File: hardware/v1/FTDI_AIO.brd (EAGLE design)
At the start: 49.5 x 49.5 mm, 45 parts, among them IC1 MCP1702-3.3, IC2 FT232RL, X1 ISP, X2 USB-A-H, X3 UART

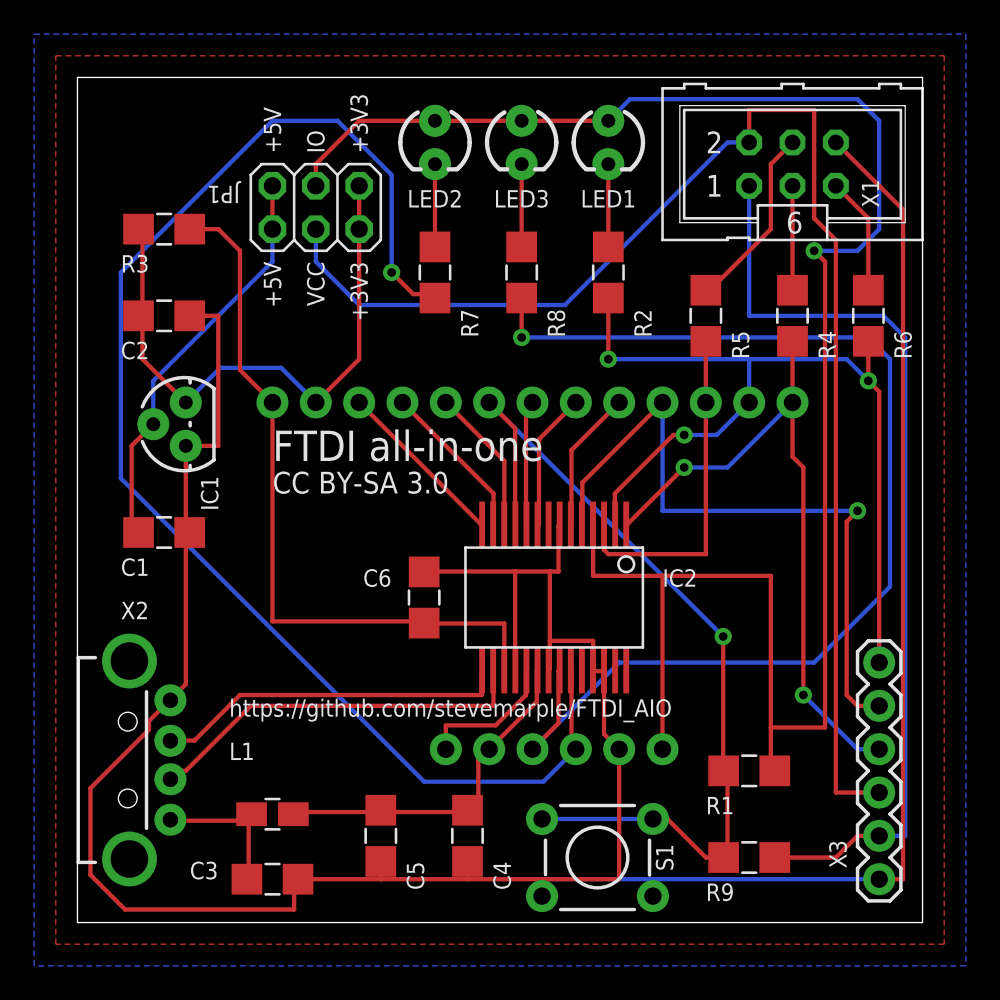
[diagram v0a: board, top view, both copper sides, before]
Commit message: Moved jumper block. Updated FT232RL package.
Jumper block moved to make room for larger text describing jumper options.
Updated FT232RL so that silkscreen does not printer over pads.
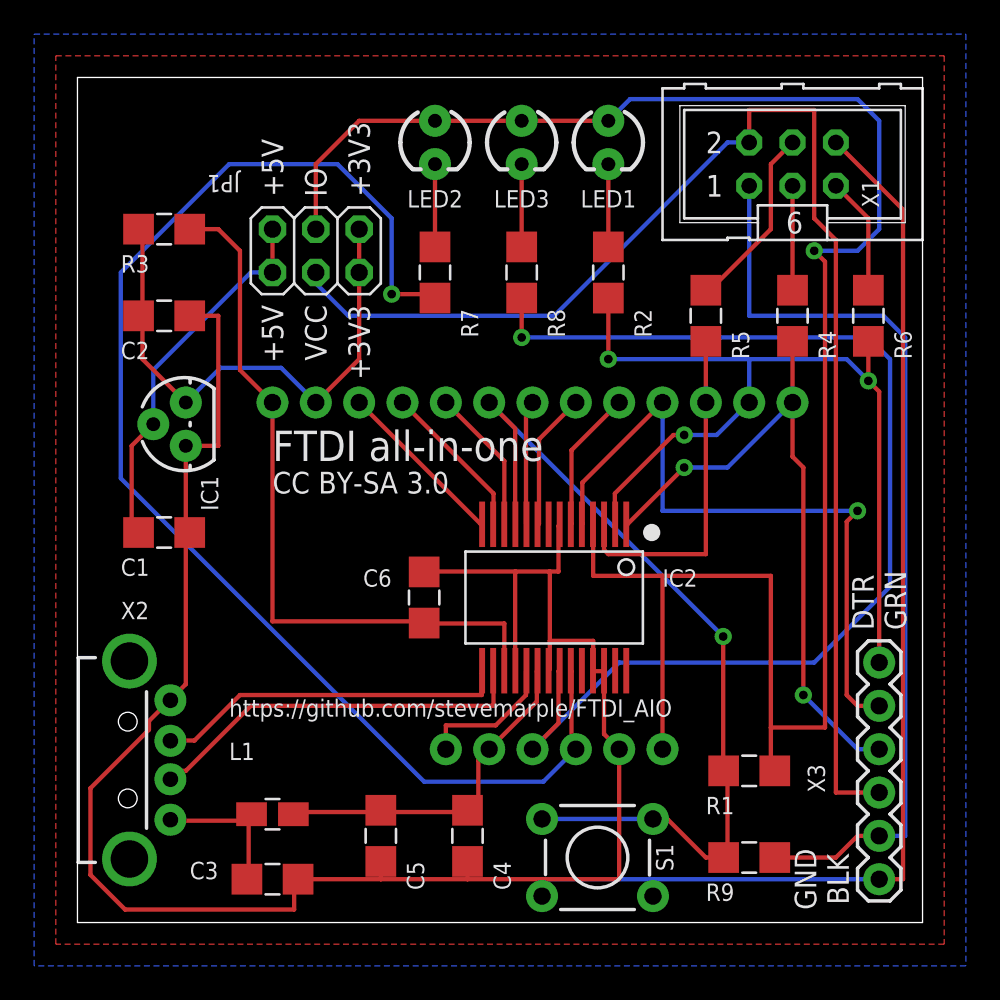
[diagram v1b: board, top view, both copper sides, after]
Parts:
- moved JP1 2.54 mm to (14.0, 39.4)
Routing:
- net N$11: track 81.5 -> 78.6 mm
- net +3V3: track 35.0 -> 32.4 mm
- net VCC: track 113.7 -> 116.3 mm
- net +5V: track 24.2 -> 22.5 mm
- net EXT_VCC: track 81.1 -> 79.8 mm
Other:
- board text added: "DTR GRN"
- board text added: "GND BLK"
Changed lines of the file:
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@@
 <wire x1="49.53" y1="49.53" x2="0" y2="49.53" width="0" layer="20"/>
 <wire x1="0" y1="49.53" x2="0" y2="0" width="0" layer="20"/>
-<text x="13.97" y="38.735" size="1.016" layer="121" ratio="10" rot="R90" align="center-right">VCC</text>
-<text x="13.97" y="45.085" size="1.016" layer="121" ratio="10" rot="R90" align="center-left">IO</text>
-<text x="11.43" y="45.085" size="1.016" layer="121" ratio="10" rot="R90" align="center-left">+5V</text>
-<text x="16.51" y="45.085" size="1.016" layer="121" ratio="10" rot="R90" align="center-left">+3V3</text>
-<text x="11.43" y="38.735" size="1.016" layer="121" ratio="10" rot="R90" align="center-right">+5V</text>
-<text x="16.51" y="38.735" size="1.016" layer="121" ratio="10" rot="R90" align="center-right">+3V3</text>
+<text x="13.97" y="36.195" size="1.27" layer="121" ratio="10" rot="R90" align="center-right">VCC</text>
+<text x="13.97" y="42.545" size="1.27" layer="121" ratio="10" rot="R90" align="center-left">IO</text>
+<text x="11.43" y="42.545" size="1.27" layer="121" ratio="10" rot="R90" align="center-left">+5V</text>
+<text x="16.51" y="42.545" size="1.27" layer="121" ratio="10" rot="R90" align="center-left">+3V3</text>
+<text x="11.43" y="36.195" size="1.27" layer="121" ratio="10" rot="R90" align="center-right">+5V</text>
+<text x="16.51" y="36.195" size="1.27" layer="121" ratio="10" rot="R90" align="center-right">+3V3</text>
 <text x="11.43" y="27.051" size="1.778" layer="121" ratio="14">FTDI all-in-one</text>
 <text x="41.91" y="14.605" size="1.016" layer="122" ratio="10" rot="MR0">https://github.com/stevemarple/FTDI_AIO</text>
@@
 Attribution-ShareAlike 3.0</text>
 <text x="8.89" y="12.065" size="1.016" layer="121" ratio="10">https://github.com/stevemarple/FTDI_AIO</text>
+<circle x="33.655" y="22.86" radius="0.508" width="0" layer="121"/>
+<text x="46.99" y="17.145" size="1.27" layer="121" ratio="10" rot="R90" align="center-left">DTR
+GRN</text>
+<text x="45.212" y="2.54" size="1.27" layer="121" ratio="10" rot="R90" align="bottom-center">GND
+BLK</text>
 </plain>
 <attributes>
@@
 </element>
 <element name="X3" library="SparkFun" package="1X06" value="UART" x="46.99" y="15.24" smashed="yes" rot="R270">
-<attribute name="NAME" x="45.085" y="3.175" size="1.016" layer="25" ratio="10" rot="R90"/>
-<attribute name="VALUE" x="45.085" y="6.35" size="1.016" layer="27" ratio="10" rot="R90"/>
+<attribute name="NAME" x="43.815" y="7.62" size="1.016" layer="25" ratio="10" rot="R90"/>
+<attribute name="VALUE" x="45.085" y="7.62" size="1.016" layer="27" ratio="10" rot="R90"/>
 </element>
 <element name="R7" library="SteveMarple" package="1206-HAND" value="560R" x="20.955" y="38.1" smashed="yes" rot="R90">
@@
 <attribute name="VALUE" x="40.005" y="1.27" size="1.016" layer="27" ratio="10"/>
 </element>
-<element name="JP1" library="pinhead" package="2X03" value="POWER" x="13.97" y="41.91" smashed="yes">
-<attribute name="NAME" x="9.525" y="43.18" size="1.016" layer="25" ratio="10" rot="SR180"/>
-<attribute name="VALUE" x="9.525" y="44.45" size="1.016" layer="27" ratio="10" rot="SR180"/>
+<element name="JP1" library="pinhead" package="2X03" value="POWER" x="13.97" y="39.37" smashed="yes">
+<attribute name="NAME" x="9.525" y="43.815" size="1.016" layer="25" ratio="10" rot="SR180"/>
+<attribute name="VALUE" x="9.525" y="45.085" size="1.016" layer="27" ratio="10" rot="SR180"/>
 </element>
 <element name="X1" library="SteveMarple" package="CONN-HARTING-ML6" value="ISP" x="41.91" y="44.45" smashed="yes">
@@
 <wire x1="30.226" y1="23.241" x2="30.215" y2="23.341" width="0.254" layer="1"/>
 <wire x1="16.51" y1="46.99" x2="13.97" y2="44.45" width="0.254" layer="1"/>
-<wire x1="13.97" y1="44.45" x2="13.97" y2="43.18" width="0.254" layer="1"/>
+<wire x1="13.97" y1="44.45" x2="13.97" y2="40.64" width="0.254" layer="1"/>
 <wire x1="20.955" y1="46.99" x2="16.51" y2="46.99" width="0.254" layer="1"/>
 <wire x1="20.955" y1="46.99" x2="26.035" y2="46.99" width="0.254" layer="1"/>
@@
 <contactref element="IC2" pad="23"/>
 <contactref element="U$14" pad="1"/>
-<wire x1="19.685" y1="36.83" x2="20.955" y2="36.83" width="0.254" layer="1"/>
 <wire x1="20.955" y1="36.83" x2="20.955" y2="36.601" width="0.254" layer="1"/>
-<wire x1="18.415" y1="38.1" x2="19.685" y2="36.83" width="0.254" layer="1"/>
-<wire x1="18.415" y1="43.815" x2="18.415" y2="38.1" width="0.254" layer="16"/>
-<wire x1="11.43" y1="46.99" x2="15.24" y2="46.99" width="0.254" layer="16"/>
-<wire x1="15.24" y1="46.99" x2="18.415" y2="43.815" width="0.254" layer="16"/>
-<wire x1="2.54" y1="38.1" x2="11.43" y2="46.99" width="0.254" layer="16"/>
+<wire x1="18.415" y1="36.83" x2="20.955" y2="36.83" width="0.254" layer="1"/>
+<wire x1="18.415" y1="41.275" x2="18.415" y2="36.83" width="0.254" layer="16"/>
+<wire x1="8.89" y1="44.45" x2="15.24" y2="44.45" width="0.254" layer="16"/>
+<wire x1="15.24" y1="44.45" x2="18.415" y2="41.275" width="0.254" layer="16"/>
+<wire x1="2.54" y1="38.1" x2="8.89" y2="44.45" width="0.254" layer="16"/>
 <wire x1="2.54" y1="26.035" x2="2.54" y2="38.1" width="0.254" layer="16"/>
 <wire x1="20.32" y1="8.255" x2="2.54" y2="26.035" width="0.254" layer="16"/>
@@
 <wire x1="29.21" y1="10.16" x2="28.956" y2="10.414" width="0.254" layer="1"/>
 <wire x1="28.956" y1="14.732" x2="28.915" y2="14.759" width="0.254" layer="1"/>
-<via x="18.415" y="38.1" extent="1-16" drill="0.508"/>
+<via x="18.415" y="36.83" extent="1-16" drill="0.508"/>
 </signal>
 <signal name="N$12">
@@
 <contactref element="IC1" pad="2"/>
 <contactref element="C1" pad="1"/>
-<wire x1="11.43" y1="43.18" x2="11.43" y2="40.64" width="0.254" layer="1"/>
+<wire x1="11.43" y1="40.64" x2="11.43" y2="38.1" width="0.254" layer="1"/>
 <wire x1="3.683" y1="22.86" x2="3.581" y2="22.86" width="0.254" layer="1"/>
 <wire x1="3.175" y1="27.94" x2="3.175" y2="22.86" width="0.254" layer="1"/>
 <wire x1="4.445" y1="29.21" x2="3.175" y2="27.94" width="0.254" layer="1"/>
 <wire x1="3.175" y1="22.86" x2="3.581" y2="22.86" width="0.254" layer="1"/>
-<wire x1="11.43" y1="38.735" x2="11.43" y2="40.64" width="0.254" layer="16"/>
-<wire x1="4.445" y1="31.75" x2="11.43" y2="38.735" width="0.254" layer="16"/>
-<wire x1="4.445" y1="29.21" x2="4.445" y2="31.75" width="0.254" layer="16"/>
+<wire x1="10.16" y1="38.1" x2="11.43" y2="38.1" width="0.254" layer="16"/>
+<wire x1="4.445" y1="32.385" x2="10.16" y2="38.1" width="0.254" layer="16"/>
+<wire x1="4.445" y1="29.21" x2="4.445" y2="32.385" width="0.254" layer="16"/>
 </signal>
 <signal name="+3V3">
@@
 <wire x1="3.81" y1="35.433" x2="3.81" y2="35.56" width="0.254" layer="1"/>
 <wire x1="3.81" y1="35.56" x2="3.581" y2="35.56" width="0.254" layer="1"/>
-<wire x1="16.51" y1="43.18" x2="16.51" y2="40.64" width="0.254" layer="1"/>
+<wire x1="16.51" y1="40.64" x2="16.51" y2="38.1" width="0.254" layer="1"/>
 <wire x1="16.51" y1="33.02" x2="13.97" y2="30.48" width="0.254" layer="1"/>
-<wire x1="16.51" y1="40.64" x2="16.51" y2="33.02" width="0.254" layer="1"/>
+<wire x1="16.51" y1="38.1" x2="16.51" y2="33.02" width="0.254" layer="1"/>
 <wire x1="3.81" y1="33.02" x2="3.81" y2="35.433" width="0.254" layer="1"/>
 <wire x1="6.35" y1="30.48" x2="3.81" y2="33.02" width="0.254" layer="1"/>
@@
 <contactref element="JP1" pad="3"/>
 <contactref element="X1" pad="2"/>
-<wire x1="28.575" y1="36.195" x2="38.1" y2="45.72" width="0.254" layer="16"/>
+<wire x1="27.94" y1="35.56" x2="38.1" y2="45.72" width="0.254" layer="16"/>
 <wire x1="38.1" y1="45.72" x2="39.37" y2="45.72" width="0.254" layer="16"/>
-<wire x1="16.51" y1="36.195" x2="28.575" y2="36.195" width="0.254" layer="16"/>
-<wire x1="13.97" y1="40.64" x2="13.97" y2="38.735" width="0.254" layer="16"/>
-<wire x1="13.97" y1="38.735" x2="16.51" y2="36.195" width="0.254" layer="16"/>
+<wire x1="15.875" y1="35.56" x2="27.94" y2="35.56" width="0.254" layer="16"/>
+<wire x1="13.97" y1="38.1" x2="13.97" y2="37.465" width="0.254" layer="16"/>
+<wire x1="13.97" y1="37.465" x2="15.875" y2="35.56" width="0.254" layer="16"/>
 <wire x1="44.45" y1="7.62" x2="46.99" y2="7.62" width="0.254" layer="1"/>
 <wire x1="44.45" y1="40.005" x2="44.45" y2="7.62" width="0.254" layer="1"/>

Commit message: Increasing power line track width to 0.012".
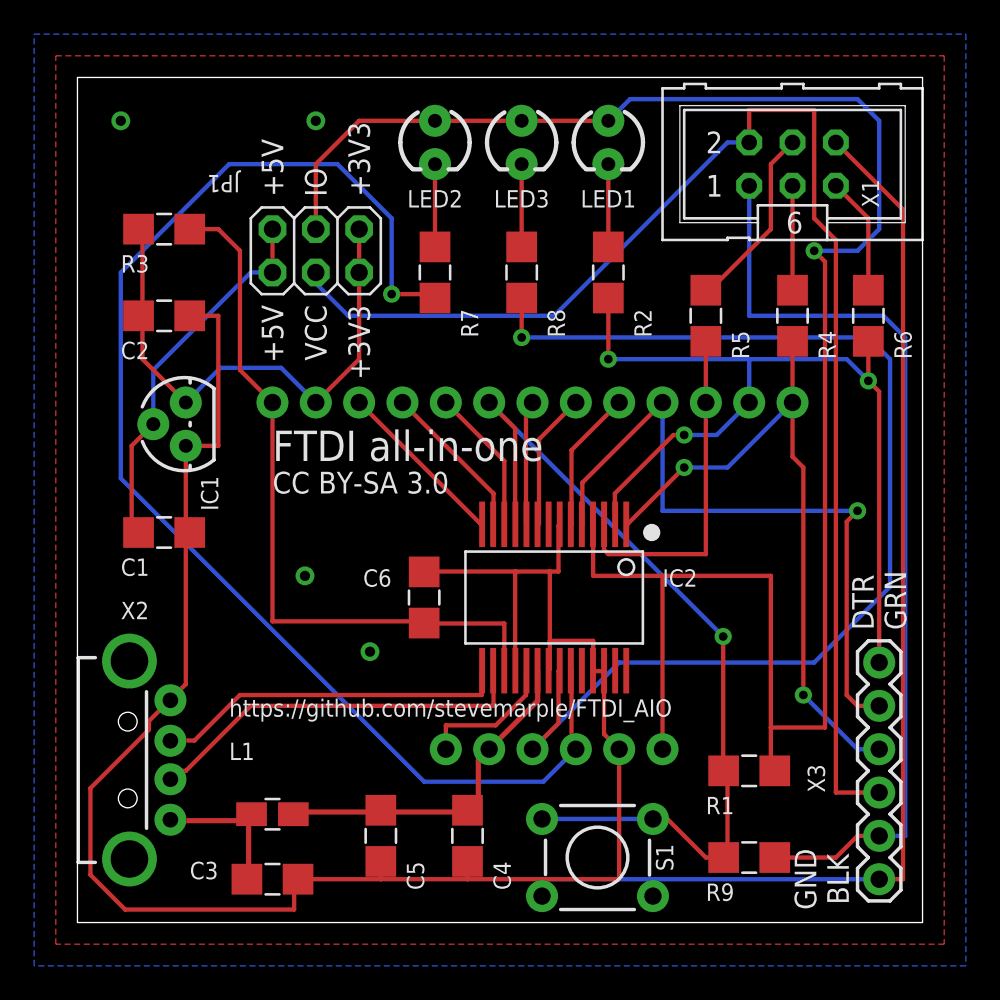
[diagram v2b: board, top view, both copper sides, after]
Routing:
- net GND: vias 0 -> 4
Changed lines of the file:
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@@
 <class number="1" name="power" width="0" drill="0">
+</class>
+<class number="2" name="Vusb_filt" width="0.3048" drill="0">
 </class>
 </classes>
@@
 <vertex x="-2.54" y="-2.54"/>
 </polygon>
+<via x="2.54" y="46.99" extent="1-16" drill="0.6"/>
+<via x="13.97" y="46.99" extent="1-16" drill="0.6"/>
+<via x="13.335" y="20.32" extent="1-16" drill="0.6"/>
+<via x="17.145" y="15.875" extent="1-16" drill="0.6"/>
 </signal>
 <signal name="TX">
@@
 <wire x1="5.461" y1="10.668" x2="5.448" y2="10.652" width="0.254" layer="1"/>
 </signal>
-<signal name="VUSB_FILT">
+<signal name="VUSB_FILT" class="2">
 <contactref element="IC2" pad="20"/>
 <contactref element="C4" pad="1"/>
@@
 <contactref element="U$4" pad="1"/>
 <contactref element="L1" pad="2"/>
-<wire x1="26.924" y1="12.954" x2="26.924" y2="14.732" width="0.254" layer="1"/>
-<wire x1="24.13" y1="10.16" x2="26.924" y2="12.954" width="0.254" layer="1"/>
-<wire x1="26.924" y1="14.732" x2="26.965" y2="14.759" width="0.254" layer="1"/>
-<wire x1="17.78" y1="6.477" x2="13.335" y2="6.477" width="0.254" layer="1"/>
-<wire x1="13.335" y1="6.477" x2="12.7" y2="6.35" width="0.254" layer="1"/>
-<wire x1="12.7" y1="6.35" x2="12.655" y2="6.35" width="0.254" layer="1"/>
-<wire x1="17.78" y1="6.477" x2="22.86" y2="6.477" width="0.254" layer="1"/>
-<wire x1="17.78" y1="6.477" x2="17.78" y2="6.579" width="0.254" layer="1"/>
-<wire x1="23.495" y1="9.525" x2="24.13" y2="10.16" width="0.254" layer="1"/>
-<wire x1="22.86" y1="6.579" x2="23.495" y2="6.604" width="0.254" layer="1"/>
-<wire x1="23.495" y1="6.604" x2="23.495" y2="9.525" width="0.254" layer="1"/>
-<wire x1="22.86" y1="6.477" x2="22.86" y2="6.579" width="0.254" layer="1"/>
-</signal>
-<signal name="VUSB">
+<wire x1="26.9748" y1="13.0048" x2="26.9748" y2="14.732" width="0.3048" layer="1"/>
+<wire x1="24.13" y1="10.16" x2="26.9748" y2="13.0048" width="0.3048" layer="1"/>
+<wire x1="26.9748" y1="14.732" x2="26.965" y2="14.759" width="0.3048" layer="1"/>
+<wire x1="17.78" y1="6.477" x2="13.335" y2="6.477" width="0.3048" layer="1"/>
+<wire x1="13.335" y1="6.477" x2="12.7" y2="6.35" width="0.3048" layer="1"/>
+<wire x1="12.7" y1="6.35" x2="12.655" y2="6.35" width="0.3048" layer="1"/>
+<wire x1="17.78" y1="6.477" x2="22.86" y2="6.477" width="0.3048" layer="1"/>
+<wire x1="17.78" y1="6.477" x2="17.78" y2="6.579" width="0.3048" layer="1"/>
+<wire x1="23.495" y1="9.525" x2="24.13" y2="10.16" width="0.3048" layer="1"/>
+<wire x1="22.86" y1="6.579" x2="23.495" y2="6.604" width="0.3048" layer="1"/>
+<wire x1="23.495" y1="6.604" x2="23.495" y2="9.525" width="0.3048" layer="1"/>
+<wire x1="22.86" y1="6.477" x2="22.86" y2="6.579" width="0.3048" layer="1"/>
+</signal>
+<signal name="VUSB" class="2">
 <contactref element="X2" pad="VBUS"/>
 <contactref element="C3" pad="1"/>
 <contactref element="L1" pad="1"/>
-<wire x1="10.033" y1="6.223" x2="10.16" y2="6.35" width="0.254" layer="1"/>
-<wire x1="10.033" y1="2.54" x2="10.033" y2="5.969" width="0.254" layer="1"/>
-<wire x1="10.033" y1="5.969" x2="10.033" y2="6.223" width="0.254" layer="1"/>
-<wire x1="10.16" y1="6.35" x2="10.205" y2="6.35" width="0.254" layer="1"/>
-<wire x1="10.033" y1="2.54" x2="9.931" y2="2.54" width="0.254" layer="1"/>
-<wire x1="5.461" y1="5.969" x2="10.033" y2="5.969" width="0.254" layer="1"/>
-<wire x1="10.033" y1="5.969" x2="10.205" y2="6.35" width="0.254" layer="1"/>
-<wire x1="5.461" y1="5.969" x2="5.448" y2="6.025" width="0.254" layer="1"/>
+<wire x1="10.033" y1="6.223" x2="10.16" y2="6.35" width="0.3048" layer="1"/>
+<wire x1="10.033" y1="2.54" x2="10.033" y2="5.969" width="0.3048" layer="1"/>
+<wire x1="10.033" y1="5.969" x2="10.033" y2="6.223" width="0.3048" layer="1"/>
+<wire x1="10.16" y1="6.35" x2="10.205" y2="6.35" width="0.3048" layer="1"/>
+<wire x1="10.033" y1="2.54" x2="9.931" y2="2.54" width="0.3048" layer="1"/>
+<wire x1="5.461" y1="5.969" x2="10.033" y2="5.969" width="0.3048" layer="1"/>
+<wire x1="10.033" y1="5.969" x2="10.205" y2="6.35" width="0.3048" layer="1"/>
+<wire x1="5.461" y1="5.969" x2="5.448" y2="6.025" width="0.3048" layer="1"/>
 </signal>
 <signal name="N$7">
